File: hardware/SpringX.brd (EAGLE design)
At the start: 30.1 x 10.8 mm, 12 parts, among them U1 MCP1703-5002E/CB, U2 MCP602ST, X1 87438-03

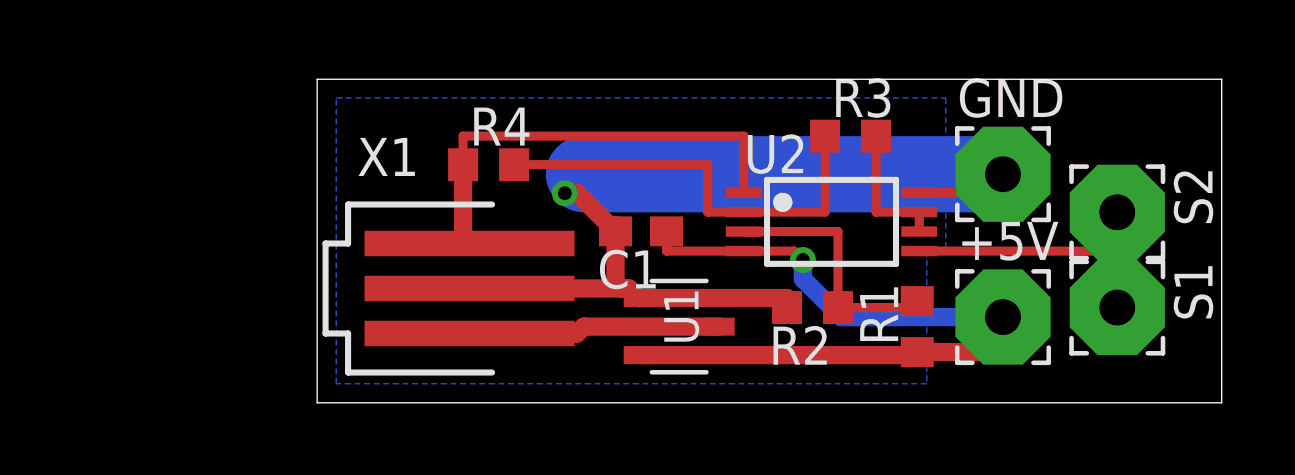
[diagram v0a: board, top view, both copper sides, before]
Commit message: minor tweaks to labels placement / size, board dimension and schematics
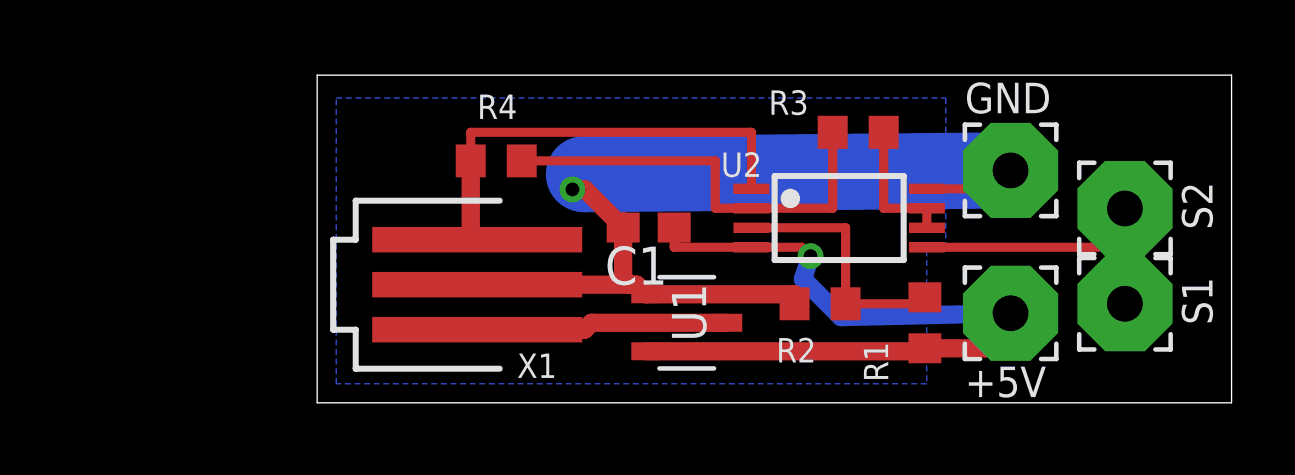
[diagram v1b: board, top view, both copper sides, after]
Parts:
- moved U2 0.28 mm to (17.4, 6.16)
- moved +5V 0.28 mm to (23.1, 2.98)
- moved GND 0.28 mm to (23.1, 7.75)
- moved U1 0.28 mm to (12.3, 2.67)
- moved R4 0.28 mm to (5.97, 8.06)
- moved C1 0.28 mm to (11.0, 5.84)
- moved X1 0.28 mm to (5.33, 3.94)
- moved S2 0.28 mm to (26.9, 6.48)
- moved R2 0.28 mm to (16.8, 3.30)
- moved S1 0.28 mm to (26.9, 3.30)
- moved R1 0.28 mm to (20.3, 2.67)
- moved R3 0.28 mm to (18.0, 9.02)
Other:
- board size 30.1 x 10.8 mm -> 30.5 x 10.9 mm

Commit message: Updated file version to Eagle 6.5.0.
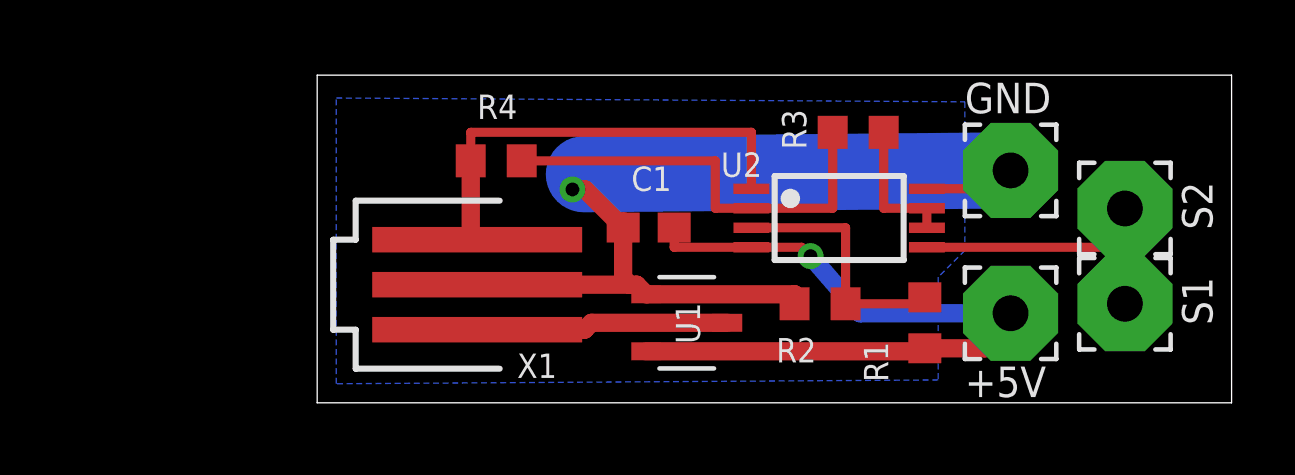
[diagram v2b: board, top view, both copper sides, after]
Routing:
- net 5V: track 26.4 -> 25.7 mm
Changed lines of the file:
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@@
 <layers>
 <layer number="1" name="Top" color="4" fill="1" visible="yes" active="yes"/>
-<layer number="16" name="Bottom" color="1" fill="1" visible="no" active="yes"/>
+<layer number="16" name="Bottom" color="1" fill="1" visible="yes" active="yes"/>
 <layer number="17" name="Pads" color="2" fill="1" visible="yes" active="yes"/>
 <layer number="18" name="Vias" color="2" fill="1" visible="yes" active="yes"/>
@@
 <elements>
 <element name="U1" library="_hhn_MCP1703" package="SOT23A_MICROCHIP_CB" value="MCP1703-5002E/CB" x="12.319" y="2.667" smashed="yes" rot="R270">
-<attribute name="NAME" x="11.824" y="3.972" size="1.143" layer="25" ratio="9" rot="R270"/>
+<attribute name="NAME" x="11.951" y="3.337" size="0.8128" layer="25" ratio="9" rot="R270"/>
 <attribute name="VALUE" x="9.044" y="3.972" size="1.143" layer="27" ratio="9" rot="R270"/>
 </element>
@@
 </element>
 <element name="R3" library="rcl" package="R0603" value="1K" x="18.034" y="9.017" smashed="yes">
-<attribute name="NAME" x="16.383" y="10.414" size="0.8128" layer="25" rot="R180"/>
+<attribute name="NAME" x="15.494" y="9.779" size="0.8128" layer="25" rot="R270"/>
 <attribute name="VALUE" x="17.399" y="7.112" size="1.27" layer="27"/>
 </element>
@@
 </element>
 <element name="C1" library="rcl" package="C0603" value="1uF" x="11.049" y="5.842" smashed="yes" rot="R180">
-<attribute name="NAME" x="11.684" y="5.207" size="1.27" layer="25" rot="R180"/>
+<attribute name="NAME" x="11.811" y="7.874" size="0.8128" layer="25" rot="R180"/>
 <attribute name="VALUE" x="11.684" y="7.747" size="1.27" layer="27" rot="R180"/>
 </element>
@@
 <polygon width="0.3048" layer="16" isolate="0.3048">
 <vertex x="0.635" y="10.16"/>
-<vertex x="20.955" y="10.16"/>
-<vertex x="20.955" y="5.08"/>
-<vertex x="20.32" y="5.08"/>
-<vertex x="20.32" y="0.635"/>
+<vertex x="21.59" y="10.033"/>
+<vertex x="21.59" y="5.08"/>
+<vertex x="20.701" y="4.191"/>
+<vertex x="20.701" y="0.762"/>
 <vertex x="0.635" y="0.635"/>
 </polygon>
@@
 <wire x1="16.1515" y1="5.1845" x2="16.4465" y2="4.8895" width="0.3048" layer="1"/>
 <via x="16.4465" y="4.8895" extent="1-16" drill="0.4572"/>
-<wire x1="16.4465" y1="4.8895" x2="16.1925" y2="4.1275" width="0.6096" layer="16"/>
-<wire x1="16.1925" y1="4.1275" x2="17.4625" y2="2.8575" width="0.6096" layer="16"/>
-<wire x1="17.4625" y1="2.8575" x2="23.114" y2="2.9845" width="0.6096" layer="16"/>
+<wire x1="16.4465" y1="4.8895" x2="18.0975" y2="2.9845" width="0.6096" layer="16"/>
+<wire x1="18.0975" y1="2.9845" x2="23.114" y2="2.9845" width="0.6096" layer="16"/>
 </signal>
 <signal name="N$4">

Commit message: Major revision to board. Corrected error - Op amp power and ground pins reversed Changed to Molex KK connector type. Complete board re-layout.
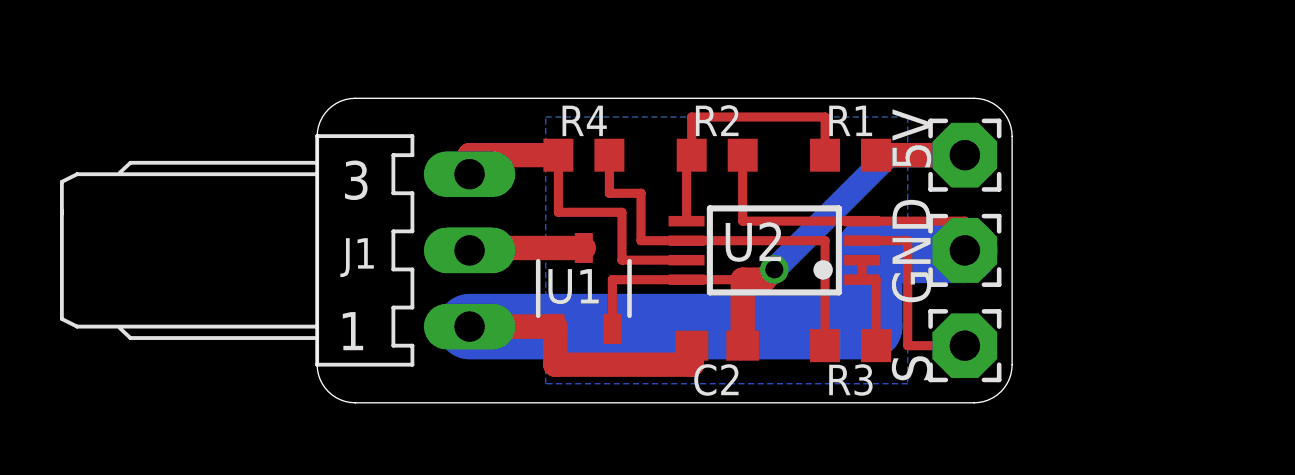
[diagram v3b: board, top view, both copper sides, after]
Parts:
- removed +5V, S1, S2: WIREPAD3,17/1,2, wirepad:3,17/1,2
- removed C1: 1uF, rcl:C0603
- removed X1: 87438-03, con-molex:87438-03
- added 5V, S: (no value), wirepad:2,15/1,0
- added C2: 1uF, rcl:C0603
- added J1: (no value), ep_molex_6410_7395-02:7395-03
- GND: value WIREPAD3,17/1,2 -> (none); device wirepad:3,17/1,2 -> wirepad:2,15/1,0
- R1, R2: value 10K -> 2.49K 0.1%
- moved R3 7.12 mm to (17.8, 1.91)
- moved R1 6.11 mm to (17.8, 8.26), turned to 180 degrees
- moved R2 6.02 mm to (13.3, 8.26), turned to 0 degrees
- moved U1 3.61 mm to (8.89, 3.81), turned to 0 degrees
- moved GND 3.07 mm to (21.6, 5.08), turned to 270 degrees
- moved R4 2.93 mm to (8.89, 8.26)
- moved U2 2.41 mm to (15.2, 5.08), turned to 90 degrees
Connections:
- removed net N$1: U1.3, X1.3
- removed net STR: S1.1, S2.1, U2.5
- new net N$3: S.1, U2.3
- new net VI: J1.2, U1.3
- net 5V: now also 5V.1, C2.1, U2.8; no longer +5V.1, C1.1, U2.4
- net GND: now also C2.2, J1.1, U2.4; no longer C1.2, U2.8, X1.2
- net N$2: now also U2.1, U2.2; no longer U2.6, U2.7
- net N$4: now also U2.6; no longer U2.2
- net OUT: now also J1.3, U2.7; no longer U2.1, X1.1
- net VREF: now also U2.5; no longer U2.3
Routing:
- net STR: track 9.77 -> 0.00 mm
- net N$1: track 8.43 -> 0.00 mm
- net N$3: track 0.00 -> 6.93 mm
- net GND: track 33.4 -> 38.9 mm, vias 1 -> 0
- net 5V: track 25.7 -> 20.3 mm
- net VI: track 0.00 -> 3.89 mm
- net OUT: track 15.0 -> 11.4 mm
- net N$2: track 4.62 -> 3.31 mm
- net N$4: track 14.5 -> 13.5 mm
- net VREF: track 8.53 -> 9.36 mm
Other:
- board size 30.5 x 10.9 mm -> 23.2 x 10.2 mm
